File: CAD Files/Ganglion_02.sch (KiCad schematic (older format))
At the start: 101 parts

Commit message: Update BOM to match new schematic refs
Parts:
- C19: renamed from C?; value 100uF -> 47uF
- gave numbers to parts that had none: 98
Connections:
- wire segments 439 -> 569
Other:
- moved on the sheet: P1, P2, P3, P4

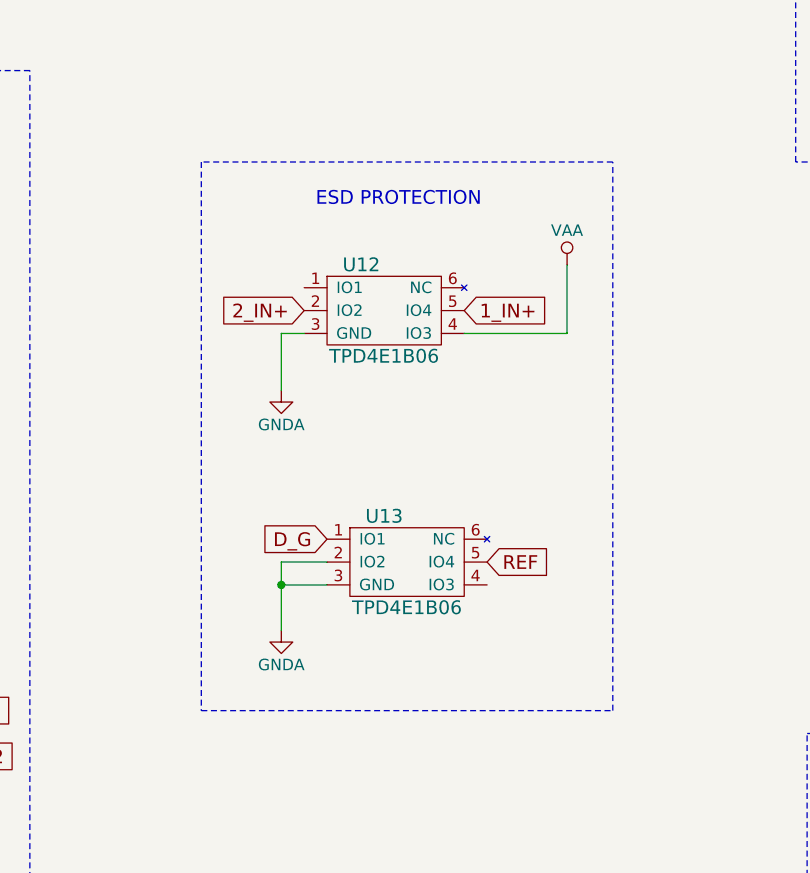
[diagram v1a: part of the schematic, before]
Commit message: Update ESD protection block
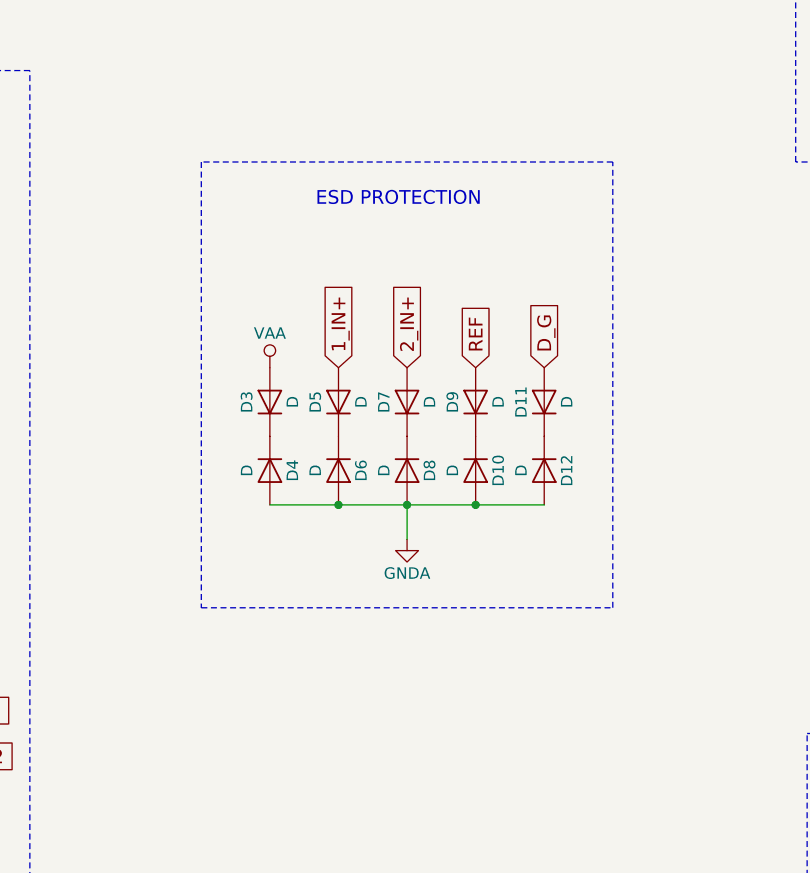
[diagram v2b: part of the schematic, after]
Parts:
- removed U12, U13: TPD4E1B06, TO_SOT_Packages_SMD:SC-70-6, symbol TPD4E1B06
- added D10, D11, D12, D3, D4, D5, D6, D7, D8, D9: D, symbol D
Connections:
- net 1_IN+: now also D5.2 (A)
- net 2_IN+: now also D7.2 (A)
- net D_G: now also D11.2 (A)
- net GNDA: now also D10.2 (A), D12.2 (A), D4.2 (A), D6.2 (A), D8.2 (A)
- net REF: now also D9.2 (A)
- net VAA: now also D3.2 (A)
- new net: D5.1 (K), D6.1 (K)
- new net: D3.1 (K), D4.1 (K)
- new net: D7.1 (K), D8.1 (K)
- new net: D10.1 (K), D9.1 (K)
- new net: D11.1 (K), D12.1 (K)

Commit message: Update instrumentation amps with DIP replacements
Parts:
- removed C30, C33: 0.1uF, Capacitors_SMD:C_0603, symbol C
- removed C31, C35: 1uF, Capacitors_SMD:C_0603, symbol C
- removed P1, P2: CONN_01X08, Socket_Strips:Socket_Strip_Straight_1x08, symbol Conn_01x08
- removed P3, P4: CONN_01X04, Socket_Strips:Socket_Strip_Straight_1x04, symbol Conn_01x04
- removed R15, R16: 100K, Resistors_SMD:R_0603, symbol R
- removed U5, U6: AD8237, Housings_SSOP:MSOP-8_3x3mm_Pitch0.65mm, symbol AD8237
- added U5, U6: AD627, symbol AD620
- R20, R21: value 2K -> 5K
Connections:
- net OUT_2 is gone; now on net OUT_1: R19.2, R27.1
- net 1_IN+: now also U5.2 (-)
- net 2_IN+: now also U6.2 (-)
- net D_23: no longer D2.2 (A)
- net GNDA: now also R31.1, U5.4 (Vs-), U6.4 (Vs-); no longer R31.2
- net OUT_1: now also R26.1, R8.1, U11.3 (CH0-), U11.4 (CH1-), U11.7 (CH2-), U11.8 (CH3-), U2.6 (-), U2.7, U5.6, U6.6
- net REF: now also U5.3 (+), U6.3 (+)
- net REF_1: now also U5.5 (Ref)
- net REF_2: now also U6.5 (Ref)
- net VAA: now also U5.7 (Vs+), U6.7 (Vs+)
- net V_IN: now also D2.2 (A)
- net at R20.1: now also U5.1 (Rg)
- net at R21.1: now also U6.1 (Rg)
- net at D2.1 (K): now also R31.2; no longer R31.1
- removed net V_REF: R20.2, R21.2, R26.1, R8.1, U11.3 (CH0-), U11.4 (CH1-), U11.7 (CH2-), U11.8 (CH3-), U2.6 (-), U2.7
- new net: R21.2, U6.8 (Rg)
- new net: R20.2, U5.8 (Rg)
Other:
- note added: "INPUTS"
- note added: "MICROCONTROLLER"
- note removed: "BREAKOUT PINS"
- note removed: "INPUT HEADER"
- note removed: "pull down here!"
- moved on the sheet: B1, C1, C11, C13, C14, C22, C23, C24, C6, C7, C8, D1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
